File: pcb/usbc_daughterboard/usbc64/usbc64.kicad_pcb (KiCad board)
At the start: 2 copper layers, 18 x 16.5 mm, 10 parts, among them J1 USB_C_Receptacle_USB2.0, J2 Conn_01x04, U1 TPD4EUSB30

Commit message: esdald05ug4 footprint
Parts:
- U1: value TPD4EUSB30 -> ESDALD05UG4; footprint Package_SON:USON-10_2.5x1.0mm_P0.5mm -> Package_DFN_QFN:UDFN-10_1.35x2.6mm_P0.5mm
- moved U1 0.30 mm to (105.0, 55.8), turned to -90 degrees
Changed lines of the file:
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@@
     )
   )
-  (footprint "Package_SON:USON-10_2.5x1.0mm_P0.5mm" (layer "F.Cu")
-    (at 105 56.1 90)
-    (descr "USON-10 2.5x1.0mm_ Pitch 0.5mm http://www.ti.com/lit/ds/symlink/tpd4e02b04.pdf")
-    (tags "USON-10 2.5x1.0mm Pitch 0.5mm")
+  (footprint "Package_DFN_QFN:UDFN-10_1.35x2.6mm_P0.5mm" (layer "F.Cu")
+    (at 105 55.8 -90)
+    (descr "http://www.st.com/content/ccc/resource/technical/document/datasheet/f2/11/8a/ed/40/31/40/56/DM00088292.pdf/files/DM00088292.pdf/jcr:content/translations/en.DM00088292.pdf")
+    (tags "UDFN 0.5 uQFN")
     (property "Sheetfile" "usbc64.kicad_sch")
     (property "Sheetname" "")
     (attr smd)
-    (fp_text reference "U1" (at 0.01829 -2.5 90) (layer "F.SilkS")
+    (fp_text reference "U1" (at 0 -2.17 90) (layer "F.SilkS")
       (effects (font (size 1 1) (thickness 0.15)))
     )
-    (fp_text value "TPD4EUSB30" (at 0.01829 2.5 90) (layer "F.Fab")
+    (fp_text value "ESDALD05UG4" (at 0 2.29 90) (layer "F.Fab")
       (effects (font (size 1 1) (thickness 0.15)))
     )
     (fp_text user "${REFERENCE}" (at 0 0) (layer "F.Fab")
-      (effects (font (size 0.55 0.55) (thickness 0.1)))
+      (effects (font (size 0.5 0.5) (thickness 0.075)))
     )
-    (fp_line (start 0.5 -1.4) (end -0.8 -1.4) (layer "F.SilkS") (width 0.12))
-    (fp_line (start 0.5 1.4) (end -0.5 1.4) (layer "F.SilkS") (width 0.12))
-    (fp_line (start -0.91 -1.5) (end 0.91 -1.5) (layer "F.CrtYd") (width 0.05))
-    (fp_line (start 0.91 1.5) (end -0.91 1.5) (layer "F.CrtYd") (width 0.05))
-    (fp_line (start -0.91 1.5) (end -0.91 -1.5) (layer "F.CrtYd") (width 0.05))
-    (fp_line (start 0.91 -1.5) (end 0.91 1.5) (layer "F.CrtYd") (width 0.05))
-    (fp_line (start 0.5 -1.25) (end -0.25 -1.25) (layer "F.Fab") (width 0.1))
-    (fp_line (start -0.5 -1) (end -0.5 1.25) (layer "F.Fab") (width 0.1))
-    (fp_line (start -0.5 1.25) (end 0.5 1.25) (layer "F.Fab") (width 0.1))
-    (fp_line (start -0.25 -1.25) (end -0.5 -1) (layer "F.Fab") (width 0.1))
-    (fp_line (start 0.5 -1.25) (end 0.5 1.25) (layer "F.Fab") (width 0.1))
-    (pad "1" smd rect (at -0.385 -1) (size 0.3 0.55) (layers "F.Cu" "F.Paste" "F.Mask")
+    (fp_line (start -0.65 1.4) (end 0.65 1.4) (layer "F.SilkS") (width 0.12))
+    (fp_line (start 0 -1.4) (end 0.65 -1.4) (layer "F.SilkS") (width 0.12))
+    (fp_circle (center -0.35 -1.1) (end -0.349999 -1.1) (layer "Dwgs.User") (width 0.12) (fill none))
+    (fp_rect (start -0.5 -1.25) (end 0.5 1.25) (layer "F.CrtYd") (width 0.12) (fill none))
+    (pad "1" smd rect (at -0.3 -1 270) (size 0.4 0.2) (layers "F.Cu" "F.Paste" "F.Mask")
       (net 15 "unconnected-(U1-Pad1)") (pinfunction "D1+") (pintype "passive"))
-    (pad "2" smd rect (at -0.385 -0.5) (size 0.3 0.55) (layers "F.Cu" "F.Paste" "F.Mask")
+    (pad "2" smd rect (at -0.3 -0.5 270) (size 0.4 0.2) (layers "F.Cu" "F.Paste" "F.Mask")
       (net 16 "unconnected-(U1-Pad2)") (pinfunction "D1-") (pintype "passive"))
-    (pad "3" smd rect (at -0.385 0) (size 0.4 0.55) (layers "F.Cu" "F.Paste" "F.Mask")
+    (pad "3" smd rect (at -0.25 0 270) (size 0.5 0.4) (layers "F.Cu" "F.Paste" "F.Mask")
       (net 23 "GNDPWR") (pinfunction "GND") (pintype "power_in"))
-    (pad "4" smd rect (at -0.385 0.5) (size 0.3 0.55) (layers "F.Cu" "F.Paste" "F.Mask")
+    (pad "4" smd rect (at -0.3 0.5 270) (size 0.4 0.2) (layers "F.Cu" "F.Paste" "F.Mask")
       (net 17 "unconnected-(U1-Pad4)") (pinfunction "D2+") (pintype "passive"))
-    (pad "5" smd rect (at -0.385 1) (size 0.3 0.55) (layers "F.Cu" "F.Paste" "F.Mask")
+    (pad "5" smd rect (at -0.3 1 270) (size 0.4 0.2) (layers "F.Cu" "F.Paste" "F.Mask")
       (net 18 "unconnected-(U1-Pad5)") (pinfunction "D2-") (pintype "passive"))
-    (pad "6" smd rect (at 0.385 1) (size 0.3 0.55) (layers "F.Cu" "F.Paste" "F.Mask")
+    (pad "6" smd rect (at 0.3 1 270) (size 0.4 0.2) (layers "F.Cu" "F.Paste" "F.Mask")
       (net 19 "unconnected-(U1-Pad6)") (pinfunction "NC") (pintype "no_connect"))
-    (pad "7" smd rect (at 0.385 0.5) (size 0.3 0.55) (layers "F.Cu" "F.Paste" "F.Mask")
+    (pad "7" smd rect (at 0.3 0.5 270) (size 0.4 0.2) (layers "F.Cu" "F.Paste" "F.Mask")
       (net 20 "unconnected-(U1-Pad7)") (pinfunction "NC") (pintype "no_connect"))
-    (pad "8" smd rect (at 0.385 0) (size 0.4 0.55) (layers "F.Cu" "F.Paste" "F.Mask")
+    (pad "8" smd rect (at 0.25 0 270) (size 0.5 0.4) (layers "F.Cu" "F.Paste" "F.Mask")
       (net 23 "GNDPWR") (pinfunction "GND") (pintype "passive"))
-    (pad "9" smd rect (at 0.385 -0.5) (size 0.3 0.55) (layers "F.Cu" "F.Paste" "F.Mask")
+    (pad "9" smd rect (at 0.3 -0.5 270) (size 0.4 0.2) (layers "F.Cu" "F.Paste" "F.Mask")
       (net 21 "unconnected-(U1-Pad9)") (pinfunction "NC") (pintype "no_connect"))
-    (pad "10" smd rect (at 0.385 -1) (size 0.3 0.55) (layers "F.Cu" "F.Paste" "F.Mask")
+    (pad "10" smd rect (at 0.3 -1 270) (size 0.4 0.2) (layers "F.Cu" "F.Paste" "F.Mask")
       (net 22 "unconnected-(U1-Pad10)") (pinfunction "NC") (pintype "no_connect"))
-    (model "${KICAD6_3DMODEL_DIR}/Package_SON.3dshapes/USON-10_2.5x1.0mm_P0.5mm.wrl"
+    (model "${KICAD6_3DMODEL_DIR}/Package_DFN_QFN.3dshapes/UDFN-10_1.35x2.6mm_P0.5mm.wrl"
       (offset (xyz 0 0 0))
-      (scale (xyz 1 1 1))
+      (scale (xyz 0.74 0.96 1.1))
       (rotate (xyz 0 0 0))
     )

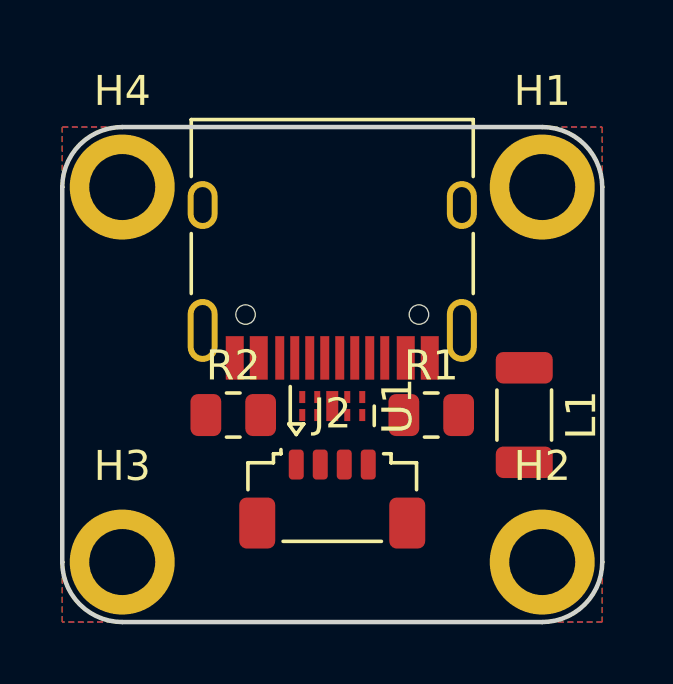
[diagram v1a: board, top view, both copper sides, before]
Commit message: NC pins to passive and tied a/b data lines
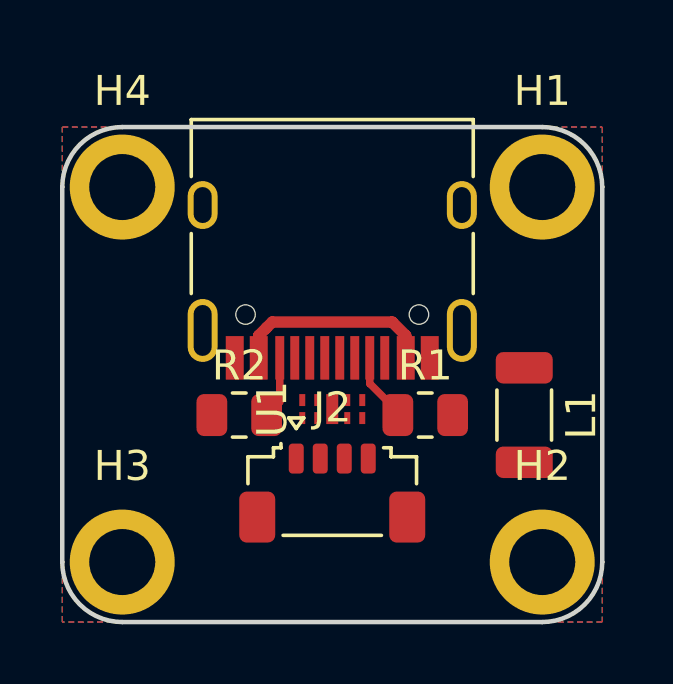
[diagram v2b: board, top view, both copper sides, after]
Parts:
- U1: footprint Package_DFN_QFN:UDFN-10_1.35x2.6mm_P0.5mm -> ESDALD05UG4:ESDALD05UG4
- moved R1 0.20 mm to (108.1, 56.1)
- moved R2 0.20 mm to (101.9, 56.1)
- moved J2 0.20 mm to (105.0, 58.7)
- moved U1 0.10 mm to (105.0, 55.9), turned to 90 degrees
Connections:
- J1 pad A6: unconnected-(J1-PadA6) -> d+
- J1 pad A7: unconnected-(J1-PadA7) -> d-
- J1 pad B6: unconnected-(J1-PadB6) -> d+
- J1 pad B7: unconnected-(J1-PadB7) -> d-
- J2 pad 1: unconnected-(J2-Pad1) -> +5V
- J2 pad 2: unconnected-(J2-Pad2) -> d-
- J2 pad 3: unconnected-(J2-Pad3) -> d+
- J2 pad 4: unconnected-(J2-Pad4) -> GND
- U1 pad 1: unconnected-(U1-Pad1) -> d+
- U1 pad 10: unconnected-(U1-Pad10) -> d+
- U1 pad 2: unconnected-(U1-Pad2) -> d-
- U1 pad 4: unconnected-(U1-Pad4) -> d+
- U1 pad 5: unconnected-(U1-Pad5) -> d-
- U1 pad 6: unconnected-(U1-Pad6) -> d-
- U1 pad 7: unconnected-(U1-Pad7) -> d+
- U1 pad 9: unconnected-(U1-Pad9) -> d-
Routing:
- net VBUS: track 0.00 -> 6.76 mm
- net Net-(J1-PadA5): track 0.00 -> 2.29 mm
- net Net-(J1-PadB5): track 0.00 -> 2.09 mm

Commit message: rotate ferrite and connect vbus
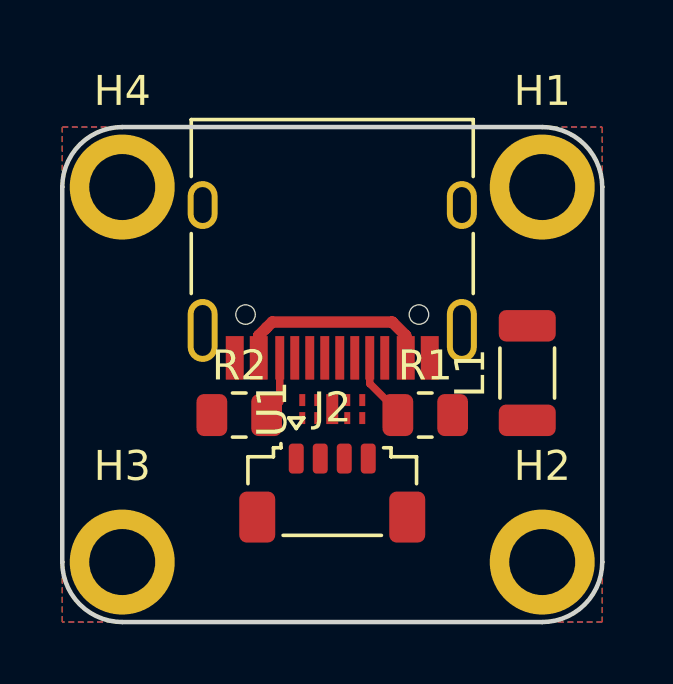
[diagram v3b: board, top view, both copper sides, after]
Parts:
- moved L1 1.40 mm to (111.5, 54.7), turned to 90 degrees
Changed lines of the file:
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@@
   (net 10 "GNDPWR")
   (footprint "Inductor_SMD:L_1206_3216Metric" (layer "F.Cu")
-    (at 111.4 56.1 -90)
+    (at 111.5 54.7 90)
     (descr "Inductor SMD 1206 (3216 Metric), square (rectangular) end terminal, IPC_7351 nominal, (Body size source: IPC-SM-782 page 80, https://www.pcb-3d.com/wordpress/wp-content/uploads/ipc-sm-782a_amendment_1_and_2.pdf), generated with kicad-footprint-generator")
     (tags "inductor")
@@
     (fp_line (start -1.6 0.8) (end -1.6 -0.8) (layer "F.Fab") (width 0.1))
     (fp_line (start -1.6 -0.8) (end 1.6 -0.8) (layer "F.Fab") (width 0.1))
-    (pad "1" smd roundrect (at -1.575 0 270) (size 1.05 1.9) (layers "F.Cu" "F.Paste" "F.Mask") (roundrect_rratio 0.238095)
+    (pad "1" smd roundrect (at -1.575 0 90) (size 1.05 1.9) (layers "F.Cu" "F.Paste" "F.Mask") (roundrect_rratio 0.238095)
       (net 1 "GND") (pintype "passive"))
-    (pad "2" smd roundrect (at 1.575 0 270) (size 1.05 1.9) (layers "F.Cu" "F.Paste" "F.Mask") (roundrect_rratio 0.238095)
+    (pad "2" smd roundrect (at 1.575 0 90) (size 1.05 1.9) (layers "F.Cu" "F.Paste" "F.Mask") (roundrect_rratio 0.238095)
       (net 10 "GNDPWR") (pintype "passive"))
     (model "${KICAD6_3DMODEL_DIR}/Inductor_SMD.3dshapes/L_1206_3216Metric.wrl"

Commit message: data traces laid
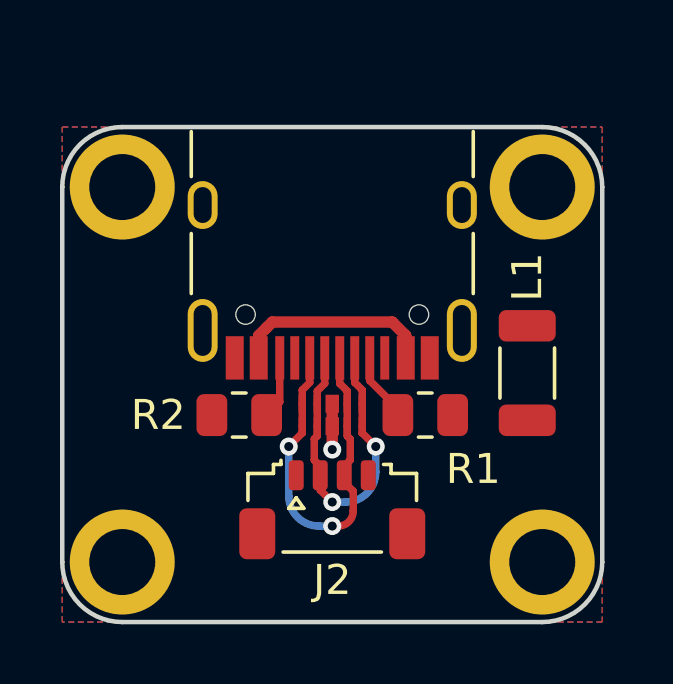
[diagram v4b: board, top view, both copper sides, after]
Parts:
- moved J2 0.56 mm to (105.0, 59.3)
- moved U1 0.20 mm to (105.0, 56.1)
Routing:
- net d+: track 0.00 -> 13.3 mm, vias 0 -> 2
- net d-: track 0.00 -> 11.3 mm, vias 0 -> 2
- net GNDPWR: track 0.00 -> 1.52 mm, vias 0 -> 1

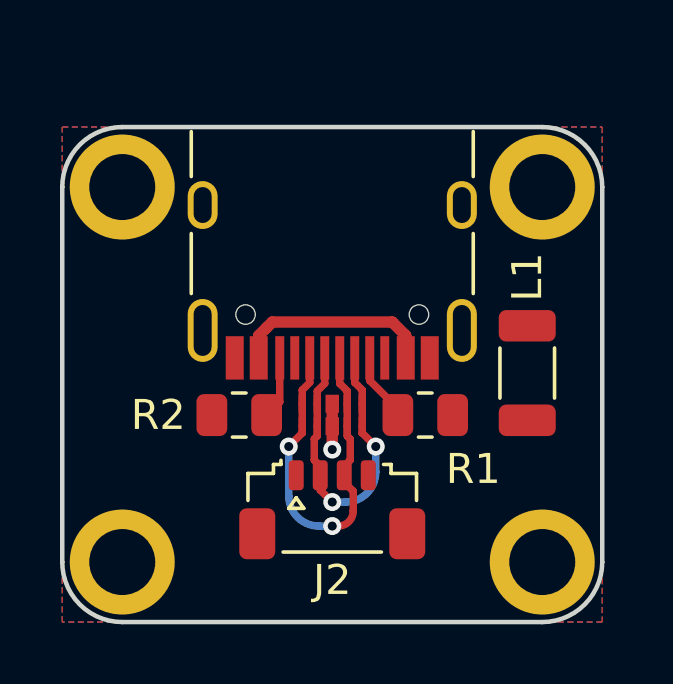
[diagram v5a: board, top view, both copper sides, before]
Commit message: silk values instead of refdes
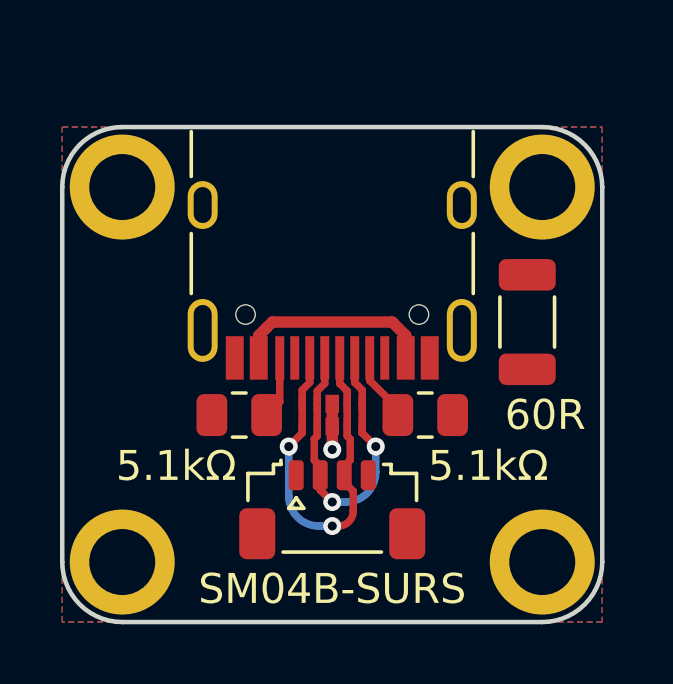
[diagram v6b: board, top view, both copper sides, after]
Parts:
- J2: value Conn_01x04 -> SM04B-SURS
- L1: value 60R@100MHz -> 60R
- moved L1 1.70 mm to (111.5, 53.0)
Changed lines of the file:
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@@
   (net 10 "GNDPWR")
   (footprint "Inductor_SMD:L_1206_3216Metric" (layer "F.Cu")
-    (at 111.5 54.7 90)
+    (at 111.5 53 90)
     (descr "Inductor SMD 1206 (3216 Metric), square (rectangular) end terminal, IPC_7351 nominal, (Body size source: IPC-SM-782 page 80, https://www.pcb-3d.com/wordpress/wp-content/uploads/ipc-sm-782a_amendment_1_and_2.pdf), generated with kicad-footprint-generator")
     (tags "inductor")
@@
     (property "Sheetname" "")
     (attr smd)
-    (fp_text reference "L1" (at 3.2 0 90) (layer "F.SilkS")
-      (effects (font (size 1 1) (thickness 0.15)))
-    )
-    (fp_text value "60R@100MHz" (at 0 1.9 90) (layer "F.Fab")
+    (fp_text reference "L1" (at 3 0 180) (layer "F.Fab")
+      (effects (font (size 1 1) (thickness 0.15)))
+    )
+    (fp_text value "60R" (at -3.1 0.6 180) (layer "F.SilkS")
       (effects (font (size 1 1) (thickness 0.15)))
     )
@@
     (property "Sheetname" "")
     (attr smd)
-    (fp_text reference "J2" (at 0 2.343223) (layer "F.SilkS")
-      (effects (font (size 1 1) (thickness 0.15)))
-    )
-    (fp_text value "Conn_01x04" (at 0 2.85) (layer "F.Fab")
+    (fp_text reference "J2" (at 0 2.343223) (layer "F.Fab")
+      (effects (font (size 1 1) (thickness 0.15)))
+    )
+    (fp_text value "SM04B-SURS" (at 0 2.643223) (layer "F.SilkS")
       (effects (font (size 1 1) (thickness 0.15)))
     )
@@
     (property "Sheetname" "")
     (attr smd)
-    (fp_text reference "R1" (at 1.6 1.8) (layer "F.SilkS")
-      (effects (font (size 1 1) (thickness 0.15)))
-    )
-    (fp_text value "5.1kΩ" (at 0 1.65) (layer "F.Fab")
+    (fp_text reference "R1" (at 2.5 2.1) (layer "F.Fab")
+      (effects (font (size 1 1) (thickness 0.15)))
+    )
+    (fp_text value "5.1kΩ" (at 2.1 1.7) (layer "F.SilkS")
       (effects (font (size 1 1) (thickness 0.15)))
     )
@@
     (property "Sheetname" "")
     (attr smd)
-    (fp_text reference "R2" (at -2.7 0) (layer "F.SilkS")
-      (effects (font (size 1 1) (thickness 0.15)))
-    )
-    (fp_text value "5.1kΩ" (at 0 1.65) (layer "F.Fab")
-      (effects (font (size 1 1) (thickness 0.15)))
-    )
+    (fp_text reference "R2" (at -2.6 2.1) (layer "F.Fab")
+      (effects (font (size 1 1) (thickness 0.15)))
+    )
+    (fp_text value "5.1kΩ" (at -2.1 1.7) (layer "F.SilkS")
+      (effects (font (size 1 1) (thickness 0.15)))
+    )

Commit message: add SH connector
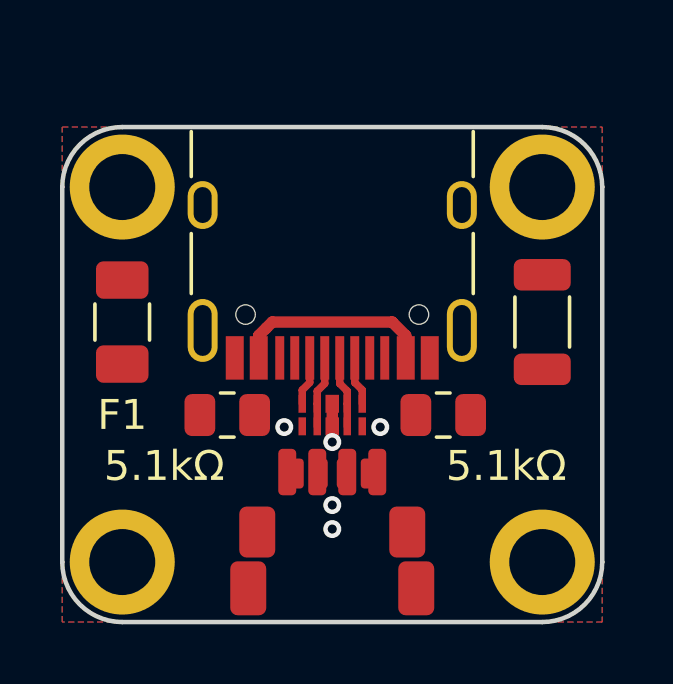
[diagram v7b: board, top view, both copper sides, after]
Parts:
- added F1: 500mA, Fuse:Fuse_1206_3216Metric, F.Cu at (98.0, 53.0)
- added J3: Conn_01x04, Connector_JST:JST_SH_SM04B-SRSS-TB_1x04-1MP_P1.00mm_Horizontal, F.Cu at (105.0, 60.0)
- J2: value SM04B-SURS -> Conn_01x04
- L1: value 60R -> 60R@100MHz
- moved R1 0.60 mm to (108.7, 56.1)
- moved L1 0.50 mm to (112.0, 53.0)
- moved R2 0.40 mm to (101.5, 56.1)
- moved J2 0.06 mm to (105.0, 59.2)
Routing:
- net d+: track 13.3 -> 4.02 mm
- net d-: track 11.3 -> 4.02 mm
- net Net-(J1-PadA5): track 2.29 -> 0.00 mm
- net Net-(J1-PadB5): track 2.09 -> 0.00 mm
- net GNDPWR: track 1.52 -> 0.75 mm
